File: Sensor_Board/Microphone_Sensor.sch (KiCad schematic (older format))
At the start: 31 parts, among them J4 Mic_Conn, U4 MAX4063

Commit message: Move Sensor Board to separate Project
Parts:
- C20, C23, C24, C25, C26, C27, CB18, CB19, CB20, CB21, CB22: footprint Capacitor_SMD:C_0603_1608Metric_Pad1.05x0.95mm_HandSolder -> Capacitor_SMD:C_0603_1608Metric_Pad1.08x0.95mm_HandSolder
- C21, C22: footprint Capacitor_SMD:C_1206_3216Metric_Pad1.42x1.75mm_HandSolder -> Capacitor_SMD:C_1206_3216Metric_Pad1.33x1.80mm_HandSolder
- R30, R31, R32, R33, R34, R35, R36, R37, R38: footprint Resistor_SMD:R_0603_1608Metric_Pad1.05x0.95mm_HandSolder -> Resistor_SMD:R_0603_1608Metric_Pad0.98x0.95mm_HandSolder

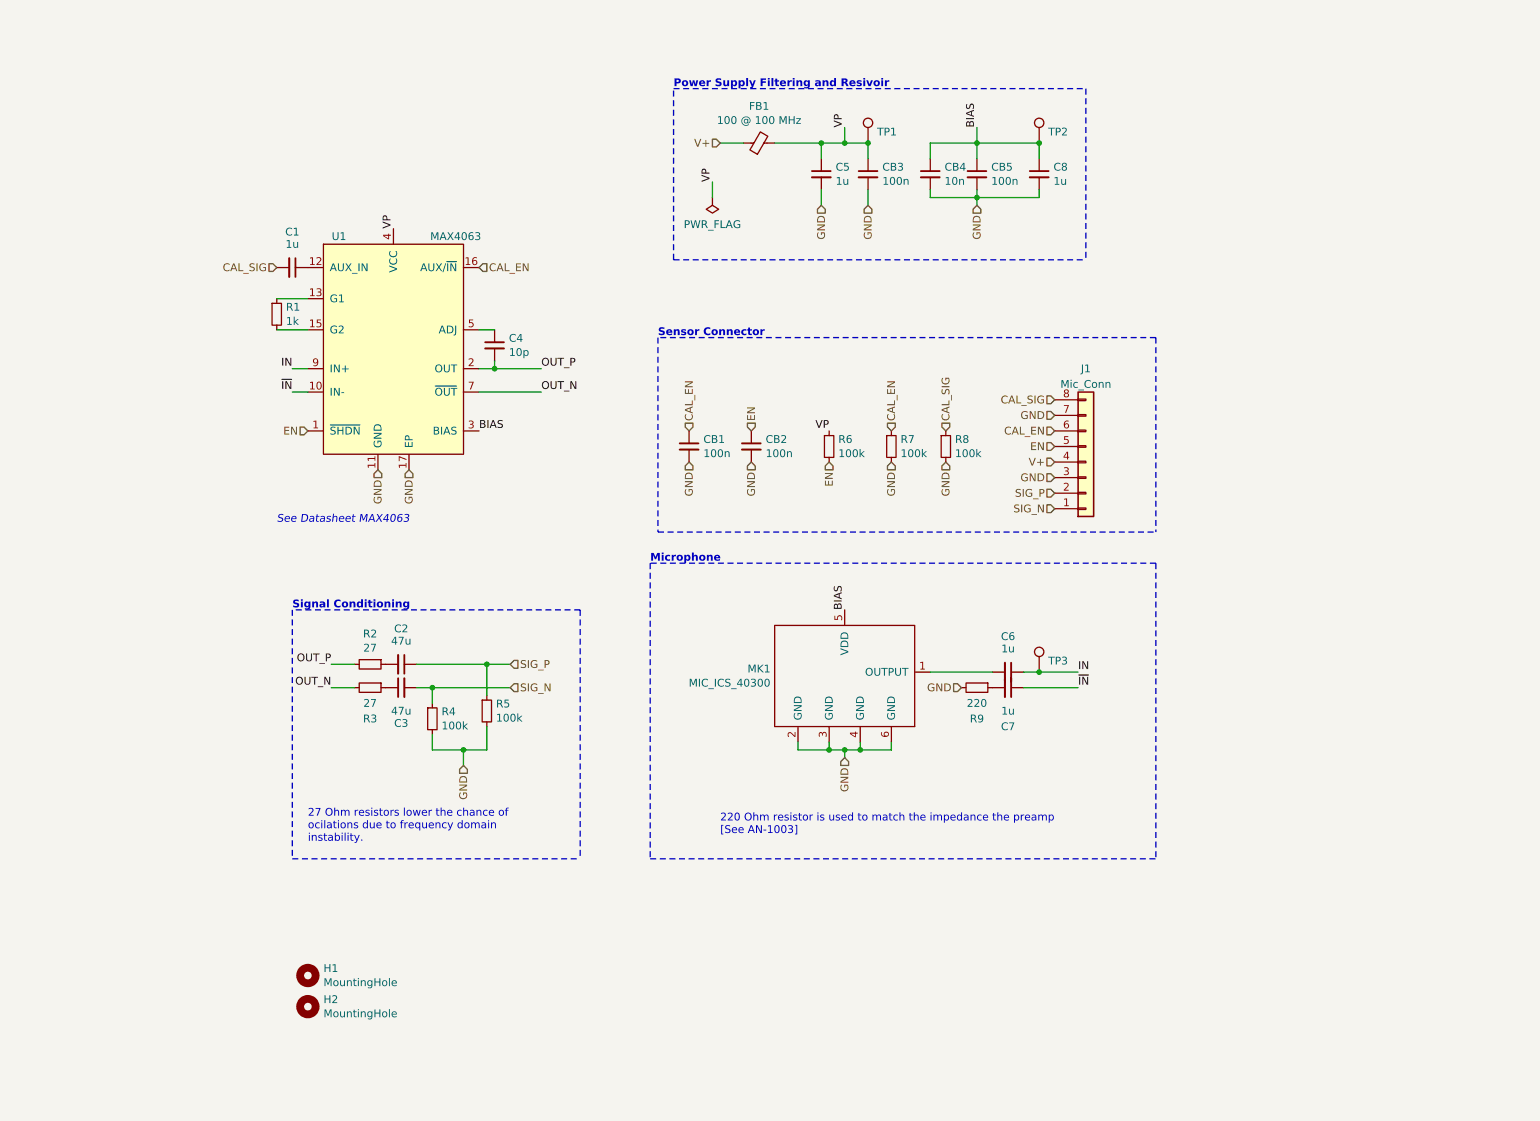
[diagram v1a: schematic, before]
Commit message: Add new preamp design
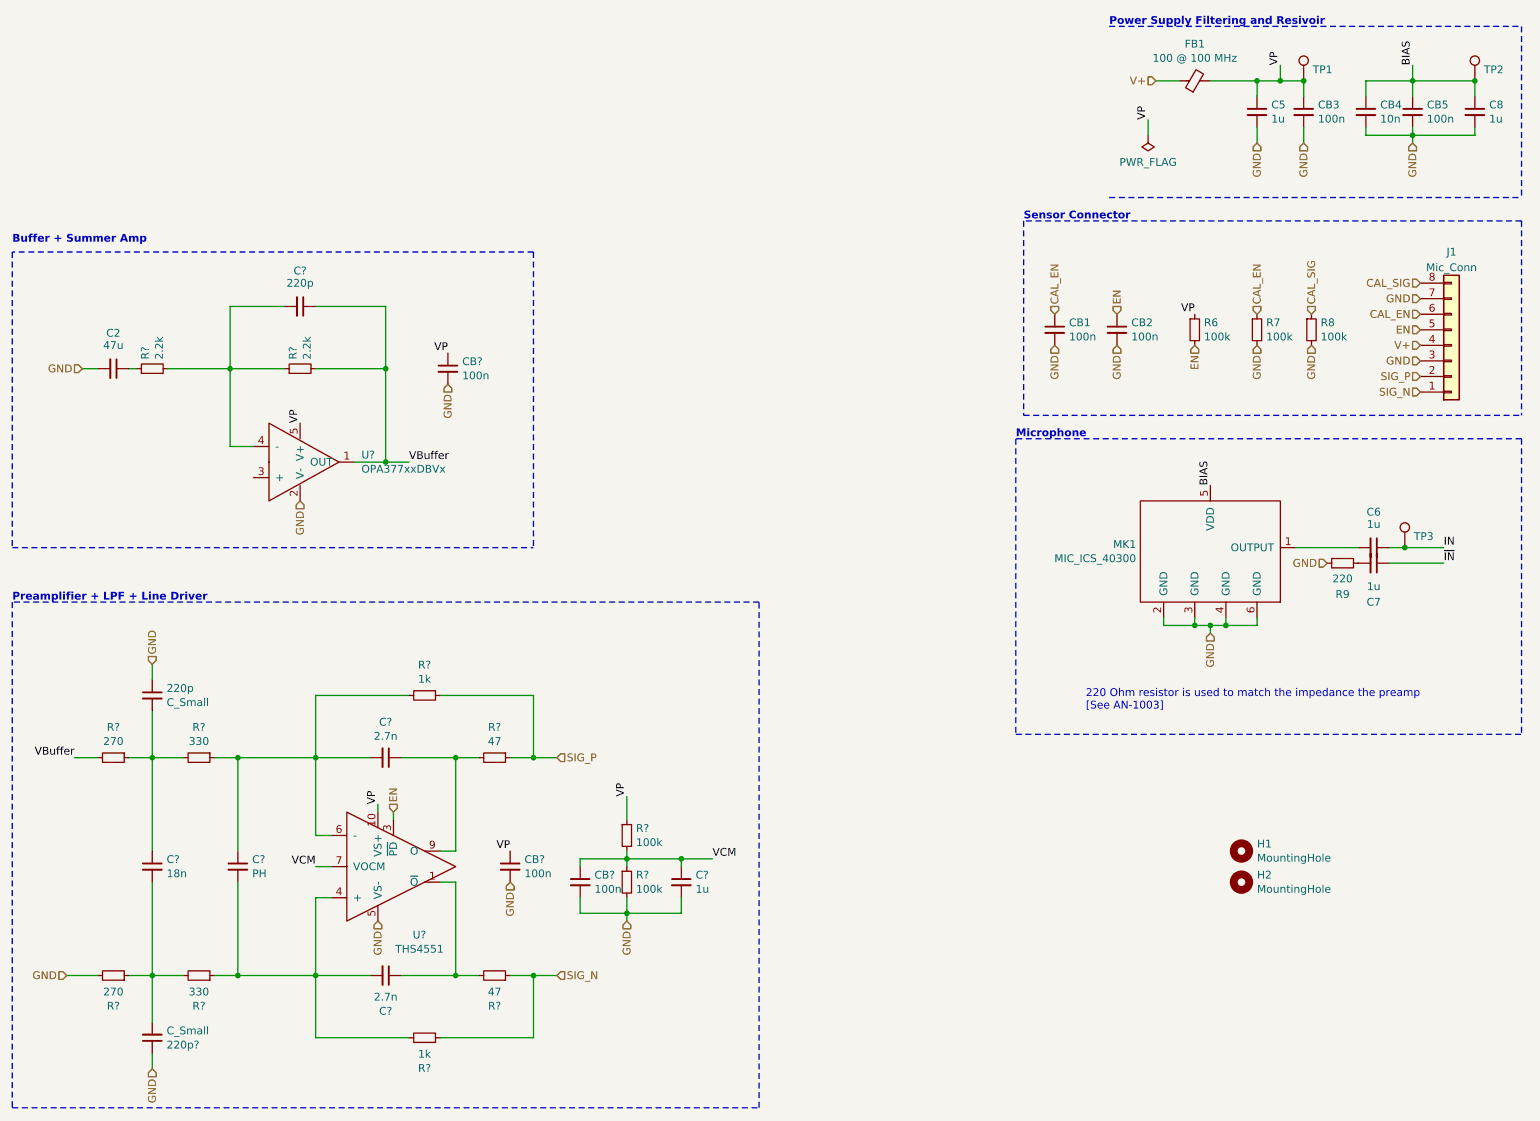
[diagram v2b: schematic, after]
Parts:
- removed C20: 1u, Capacitor_SMD:C_0603_1608Metric_Pad1.08x0.95mm_HandSolder, symbol Device:C_Small
- removed C22: 47u, Capacitor_SMD:C_1206_3216Metric_Pad1.33x1.80mm_HandSolder, symbol Device:C_Small
- removed C23: 10p, Capacitor_SMD:C_0603_1608Metric_Pad1.08x0.95mm_HandSolder, symbol Device:C_Small
- removed R30: 1k, Resistor_SMD:R_0603_1608Metric_Pad0.98x0.95mm_HandSolder, symbol Device:R_Small
- removed R31, R32: 27, Resistor_SMD:R_0603_1608Metric_Pad0.98x0.95mm_HandSolder, symbol Device:R_Small
- removed R33, R34: 100k, Resistor_SMD:R_0603_1608Metric_Pad0.98x0.95mm_HandSolder, symbol Device:R_Small
- removed U4: MAX4063, grootvoet:TQFN-16-T1644++4, symbol grootvoet:MAX4063
- added 220p, 220p?: C_Small, symbol Device:C_Small
- added C?: 220p, Capacitor_SMD:C_1206_3216Metric_Pad1.33x1.80mm_HandSolder, symbol Device:C_Small
- added C?: 1u, Capacitor_SMD:C_0603_1608Metric_Pad1.08x0.95mm_HandSolder, symbol Device:C_Small
- added C? (x2): 2.7n, symbol Device:C_Small
- added C?: PH, symbol Device:C_Small
- added C?: 18n, symbol Device:C_Small
- added CB? (x3): 100n, Capacitor_SMD:C_0603_1608Metric_Pad1.08x0.95mm_HandSolder, symbol Device:C_Small
- added R? (x2): 2.2k, Resistor_SMD:R_0603_1608Metric_Pad0.98x0.95mm_HandSolder, symbol Device:R_Small
- added R? (x2): 100k, Resistor_SMD:R_0603_1608Metric_Pad0.98x0.95mm_HandSolder, symbol Device:R_Small
- added R? (x2): 270, symbol Device:R_Small
- added R? (x2): 330, symbol Device:R_Small
- added R? (x2): 1k, symbol Device:R_Small
- added R? (x2): 47, symbol Device:R_Small
- added U?: OPA377xxDBVx, symbol grootvoet:OPA377xxDBVx
- added U?: THS4551, symbol grootvoet:THS4551
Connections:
- net EN: now also U?.3 (~PD)
- net GND: now also C21.2, 220p.1, 220p?.1, C?.2, CB?.2, CB?.2, CB?.2, R?.2, R?.2, U?.2 (V-), U?.5 (VS-)
- net SIG_N: now also R?.1, R?.1
- net SIG_P: now also R?.1, R?.1; no longer C21.1
- net VP: now also CB?.1, CB?.1, R?.1, U?.10 (VS+), U?.5 (V+)
- new net: C21.1, R?.1
- new net: C?.2, R?.1, R?.2, U?.4 (-)
- new net: C?.1, R?.2, U?.1 (~O)
- new net: C?.2, C?.2, R?.1, R?.2, U?.4 (+)
- new net: C?.1, C?.2, R?.1, R?.2, U?.6 (-)
- new net: C?.1, R?.2, U?.9 (O)
- new net: 220p.2, C?.1, R?.1, R?.2
- new net: 220p?.2, C?.2, R?.1, R?.2
- new net VBuffer: C?.1, R?.2, R?.2, U?.1 (OUT)
- new net VCM: C?.1, CB?.1, R?.1, R?.2, U?.7 (VOCM)
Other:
- note added: "Buffer + Summer Amp"
- note added: "Preamplifier + LPF + Line Driver"
- note removed: "27 Ohm resistors lower the chance of \nocilations due to frequency domain \ninstability."
- note removed: "See Datasheet MAX4063"
- note removed: "Signal Conditioning"
- moved on the sheet: C2, C5, C6, C7, C8, CB1, CB2, CB3, CB4, CB5, FB1, H1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
